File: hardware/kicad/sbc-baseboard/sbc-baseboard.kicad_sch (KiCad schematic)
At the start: 4 parts

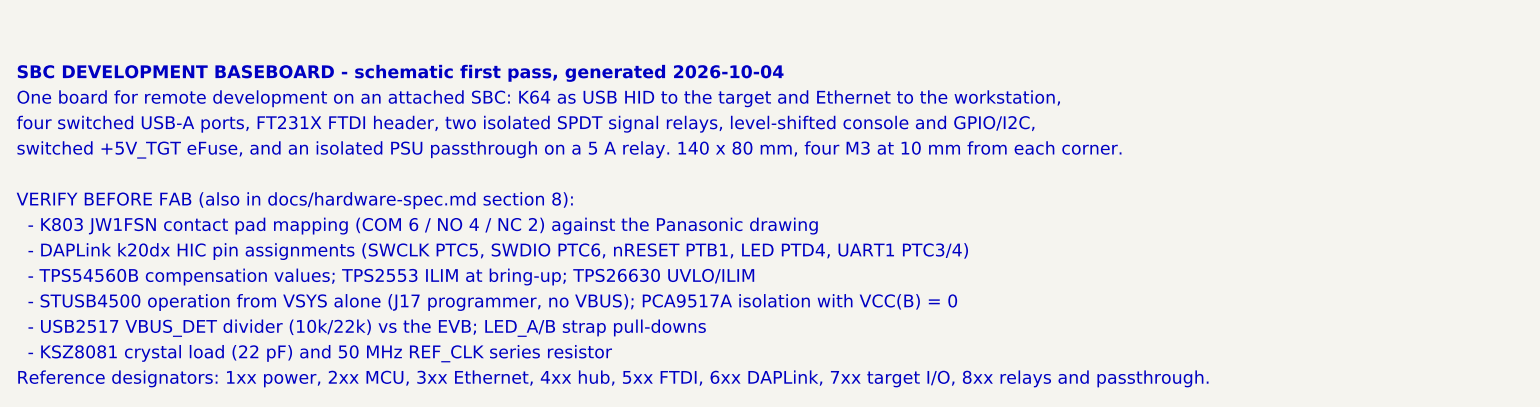
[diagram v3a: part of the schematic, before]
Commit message: Nothing drawn over anything else; FTDI Friend header; DAPLink per FRDM-K64F; 90 ohm USB class
Geometry gate now also reports two wires sharing a stretch, and is at zero on
every sheet. Routes into a stacked connector from one side take staggered
columns and rows; the signal relays are flipped so COM meets the header's
first pin without crossings; the opto-isolator moves above the passthrough
wires and taps the relay's COM lane; a tag before a route ends at the route's
target; routes into joined pins end at the join; the K64's VREGIN diode taps
the VBUS lane beside the ESD's stub; symbol mirrors are applied after
rotation, as KiCad does.

FT231X: the 3V3OUT lane stays on its pin row with its capacitor far out, clear
of the VCC decoupling; J9 mirrors the Adafruit FTDI Friend (VCC 5 V and pin 6
RTS by default on bridged solder jumpers; the first pass had left J9's VCC on
an open jumper only).

DAPLink K20, verified against DAPLink k20dx and the FRDM-K64F OpenSDA circuit:
PTC7 (SWDIO_IN) joins the SWDIO net, 33 R series resistors on the K20's USB
pair (K20_USB_P/N), notes and spec questions 12 and 14 resolved.

USB net class: 0.35 mm / 0.20 mm for 90 ohm on Advanced Circuits' standard
4-layer 62 mil stackup (spec section 8a). ERC 0, geometry 0, merges 0, layout
0, builds reproducible.

Co-Authored-By: Claude Fable 5.1 <noreply@anthropic.com>
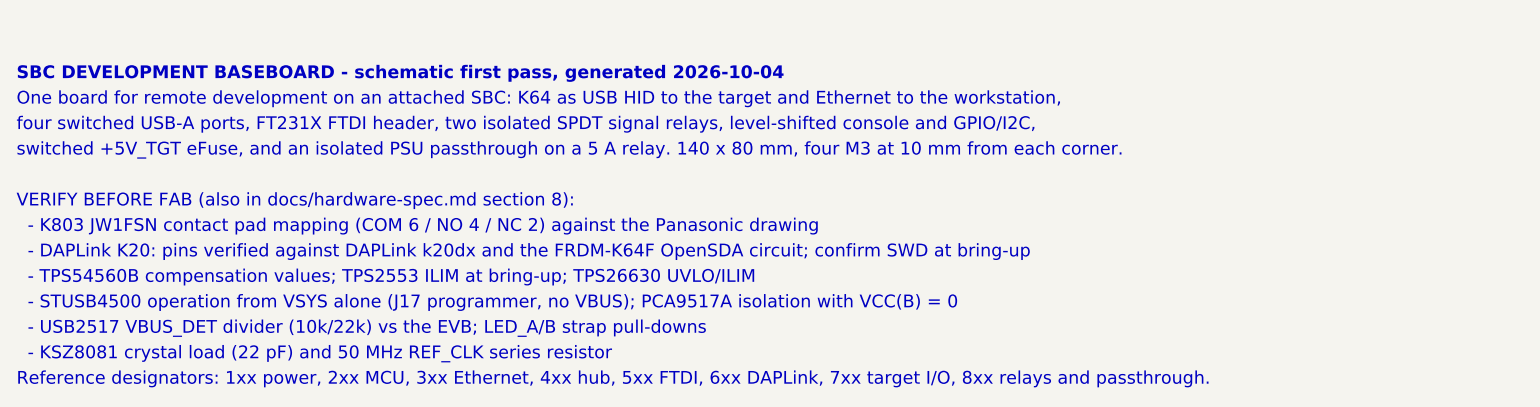
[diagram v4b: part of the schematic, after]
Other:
- note added: "- DAPLink K20: pins verified against DAPLink k20dx and the FRDM-K64F OpenSDA circuit; confirm SWD at bring-up"
- note removed: "- DAPLink k20dx HIC pin assignments (SWCLK PTC5, SWDIO PTC6, nRESET PTB1, LED PTD4, UART1 PTC3/4)"
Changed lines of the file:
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@@
 		)
 	)
-	(text "  - DAPLink k20dx HIC pin assignments (SWCLK PTC5, SWDIO PTC6, nRESET PTB1, LED PTD4, UART1 PTC3/4)"
+	(text "  - DAPLink K20: pins verified against DAPLink k20dx and the FRDM-K64F OpenSDA circuit; confirm SWD at bring-up"
 		(exclude_from_sim no)
 		(at 30 197.4 0)

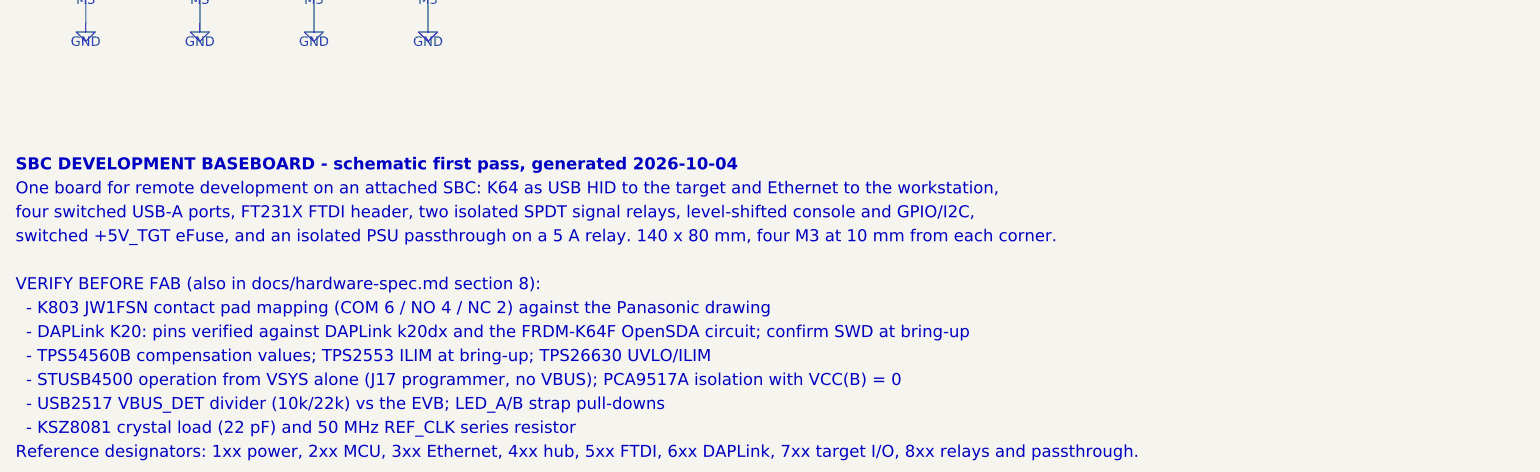
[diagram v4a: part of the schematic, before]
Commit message: Placement pass per the layout standard: connectors locked, holes at 7 mm, ICs anchored, every other part at the pin it serves
gen/pcb.py places by ecad-standards/layout.md section 3: the edge connectors
stay where the directives put them; the mounting holes move out to 7 mm from
each corner (10.5 mm corner keep-outs); the ICs are anchored by flow in
gen/layout.py and the generator refuses an anchor table that overlaps or
stands in a keep-out; every other part is placed at the pin it serves, its
host the placed part it shares the most specific nets with (a decoupling
capacitor's host is the IC the schematic draws it beside), on the host's
nearest side, two-pin parts turned to face it, packed outward in rings, in
five passes (small decoupling, the large parts on the pins, bulk, the small
parts on the pins, passive-hosted), with the nearest free spot as the
fallback. The silkscreen pass places every designator where it overlaps
nothing and omits it otherwise; ICs and connectors are never omitted.
placement.txt records every part's host and ring.

The board file, the DRC report and the placement report are byte-identical
between generations: footprints, graphics and zones are written in a sorted
order with UUIDs derived in document order, the DRC report's entries are
sorted and the USB-C's coincident pads named one way.

DRC: 12 errors, all the documented GCT USB-C hole clearances; 499 unrouted;
zero warnings. Directives, spec, README and the root-sheet note updated for
the 7 mm holes and the placement method.

Co-Authored-By: Claude Fable 5.1 <noreply@anthropic.com>
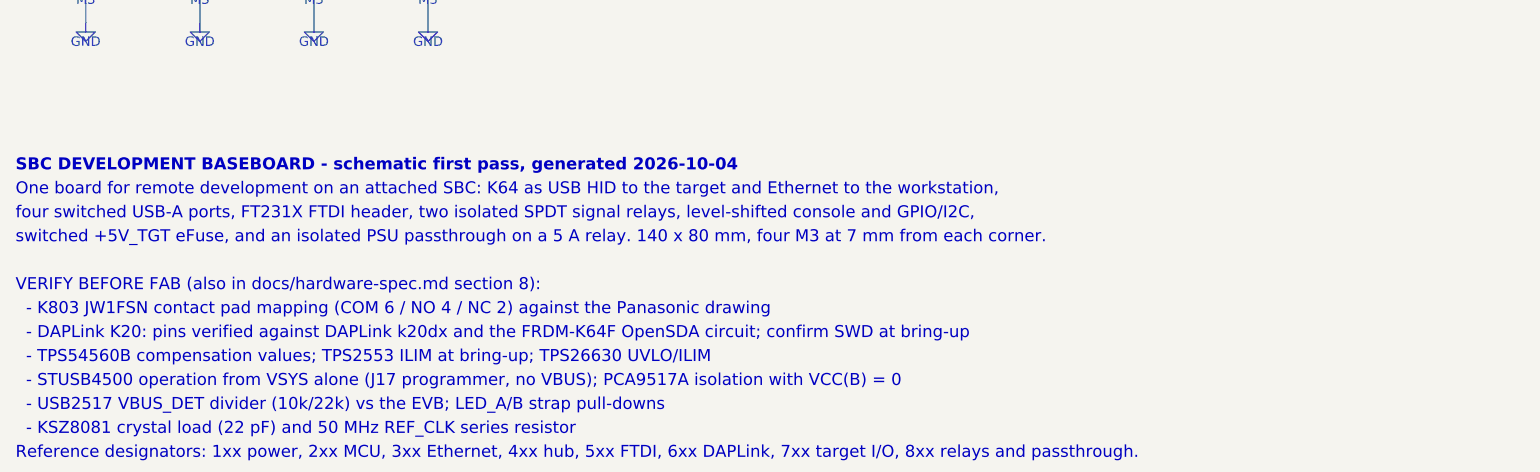
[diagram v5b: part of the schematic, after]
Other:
- note added: "switched +5V_TGT eFuse, and an isolated PSU passthrough on a 5 A relay. 140 x 80 mm, four M3 at 7 mm from each corner."
- note removed: "switched +5V_TGT eFuse, and an isolated PSU passthrough on a 5 A relay. 140 x 80 mm, four M3 at 10 mm from each corner."
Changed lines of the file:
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@@
 		)
 	)
-	(text "switched +5V_TGT eFuse, and an isolated PSU passthrough on a 5 A relay. 140 x 80 mm, four M3 at 10 mm from each corner."
+	(text "switched +5V_TGT eFuse, and an isolated PSU passthrough on a 5 A relay. 140 x 80 mm, four M3 at 7 mm from each corner."
 		(exclude_from_sim no)
 		(at 30 184.6 0)

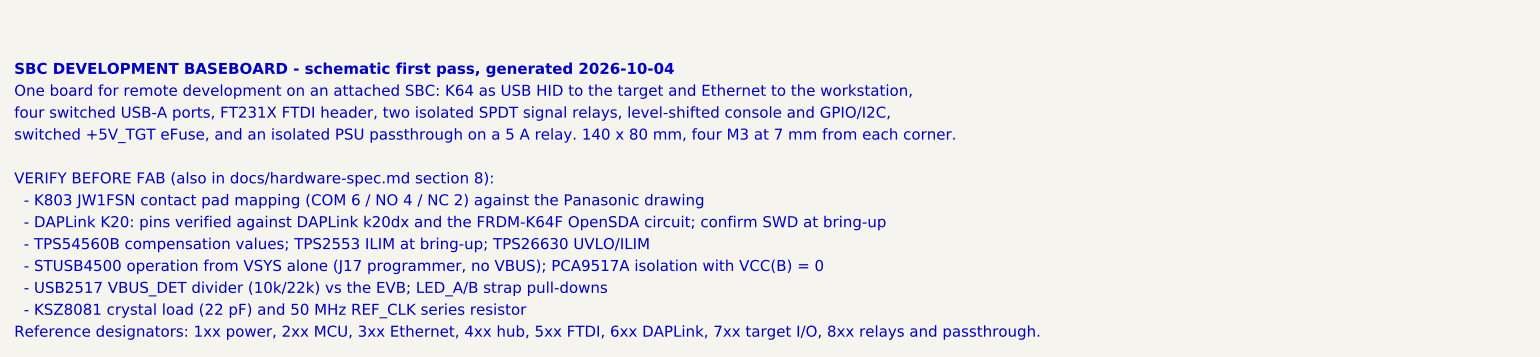
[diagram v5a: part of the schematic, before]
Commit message: The PD inlet and the two 5 V bucks go; a 2.5 mm barrel jack feeds one +5V rail through a reverse-polarity FET
Power in is a 5 V 4 A (20 W) adapter on a Kycon KLDX-0202-BC barrel
jack (J2, centre positive), clamped by an SMAJ5.0A, passed by a
DMP3013SFV P-channel MOSFET (body diode toward the rail, gate at GND,
9.5 mOhm) into +5V: two 47 uF and a 100 nF, an amber LED. The
STUSB4500, its I2C buffer and Qwiic programming header, the two
TPS54560B bucks and their islands, VBUS_IN, +5V_PORTS and +5V_TGT as
separate rails are gone; +5V feeds the port switches, the relays, the
FTDI switch, the 3V3 buck and the TPS26630 eFuse, whose output is the
switched target rail +5V_TGT, now limited to 3 A (RILIM 6.04k, the
datasheet's 18 kOhm.A / IOL). The K64's I2C0 and PD pins are freed.
Classes: PWR_4A (2.5 mm, 1.0 mm vias) for +5V and +5V_TGT in place of
PWR_6A; USB_VBUS_3A keeps the port and FTDI VBUS nets. The directives
anchor the FET behind the jack, drop the bucks' and the PD controller's
templates, and draw the one +5V rail on L4 from the jack to the eFuse.
ERC clean; the placement passes every gate, 481 connections to route.

Co-Authored-By: Claude Fable 5.1 <noreply@anthropic.com>
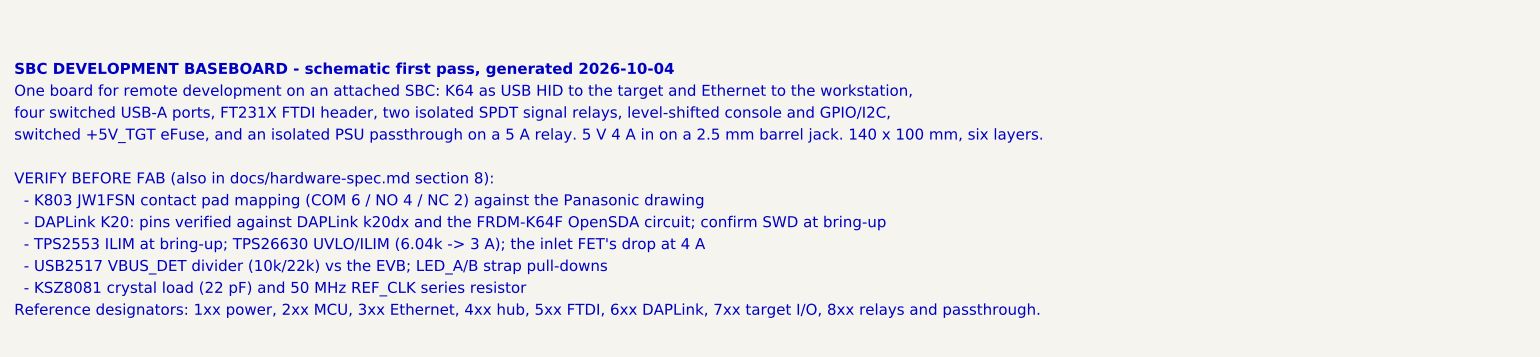
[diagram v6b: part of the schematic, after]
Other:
- note added: "- TPS2553 ILIM at bring-up; TPS26630 UVLO/ILIM (6.04k -> 3 A); the inlet FET's drop at 4 A"
- note added: "switched +5V_TGT eFuse, and an isolated PSU passthrough on a 5 A relay. 5 V 4 A in on a 2.5 mm barrel jack. 140 x 100 mm, six layers."
- note removed: "- STUSB4500 operation from VSYS alone (J17 programmer, no VBUS); PCA9517A isolation with VCC(B) = 0"
- note removed: "- TPS54560B compensation values; TPS2553 ILIM at bring-up; TPS26630 UVLO/ILIM"
- note removed: "switched +5V_TGT eFuse, and an isolated PSU passthrough on a 5 A relay. 140 x 80 mm, four M3 at 7 mm from each corner."
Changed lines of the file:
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@@
 		)
 	)
-	(text "switched +5V_TGT eFuse, and an isolated PSU passthrough on a 5 A relay. 140 x 80 mm, four M3 at 7 mm from each corner."
+	(text "switched +5V_TGT eFuse, and an isolated PSU passthrough on a 5 A relay. 5 V 4 A in on a 2.5 mm barrel jack. 140 x 100 mm, six layers."
 		(exclude_from_sim no)
 		(at 30 184.6 0)
@@
 		)
 	)
-	(text "  - TPS54560B compensation values; TPS2553 ILIM at bring-up; TPS26630 UVLO/ILIM"
+	(text "  - TPS2553 ILIM at bring-up; TPS26630 UVLO/ILIM (6.04k -> 3 A); the inlet FET's drop at 4 A"
 		(exclude_from_sim no)
 		(at 30 200.6 0)
@@
 		)
 	)
-	(text "  - STUSB4500 operation from VSYS alone (J17 programmer, no VBUS); PCA9517A isolation with VCC(B) = 0"
+	(text "  - USB2517 VBUS_DET divider (10k/22k) vs the EVB; LED_A/B strap pull-downs"
 		(exclude_from_sim no)
 		(at 30 203.8 0)
@@
 		)
 	)
-	(text "  - USB2517 VBUS_DET divider (10k/22k) vs the EVB; LED_A/B strap pull-downs"
+	(text "  - KSZ8081 crystal load (22 pF) and 50 MHz REF_CLK series resistor"
 		(exclude_from_sim no)
 		(at 30 207 0)
@@
 		)
 	)
-	(text "  - KSZ8081 crystal load (22 pF) and 50 MHz REF_CLK series resistor"
+	(text "Reference designators: 1xx power, 2xx MCU, 3xx Ethernet, 4xx hub, 5xx FTDI, 6xx DAPLink, 7xx target I/O, 8xx relays and passthrough."
 		(exclude_from_sim no)
 		(at 30 210.2 0)
 		(effects
 			(font
-				(size 1.6 1.6)
-			)
-			(justify left bottom)
-		)
-	)
-	(text "Reference designators: 1xx power, 2xx MCU, 3xx Ethernet, 4xx hub, 5xx FTDI, 6xx DAPLink, 7xx target I/O, 8xx relays and passthrough."
-		(exclude_from_sim no)
-		(at 30 213.4 0)
-		(effects
-			(font
